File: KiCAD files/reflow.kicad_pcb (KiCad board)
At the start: 2 copper layers, 58.4 x 101.6 mm, 53 parts, among them J1 Screw_Terminal_01x02, J2 Screw_Terminal_01x02, J3 Conn_01x06_Female, J4 Conn_01x06_Female, J5 Conn_01x06_Female, J6 Screw_Terminal_01x02, J7 Screw_Terminal_01x02, U1 MOC3063M, U2 HLK-PM03, U3 ESP-12E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

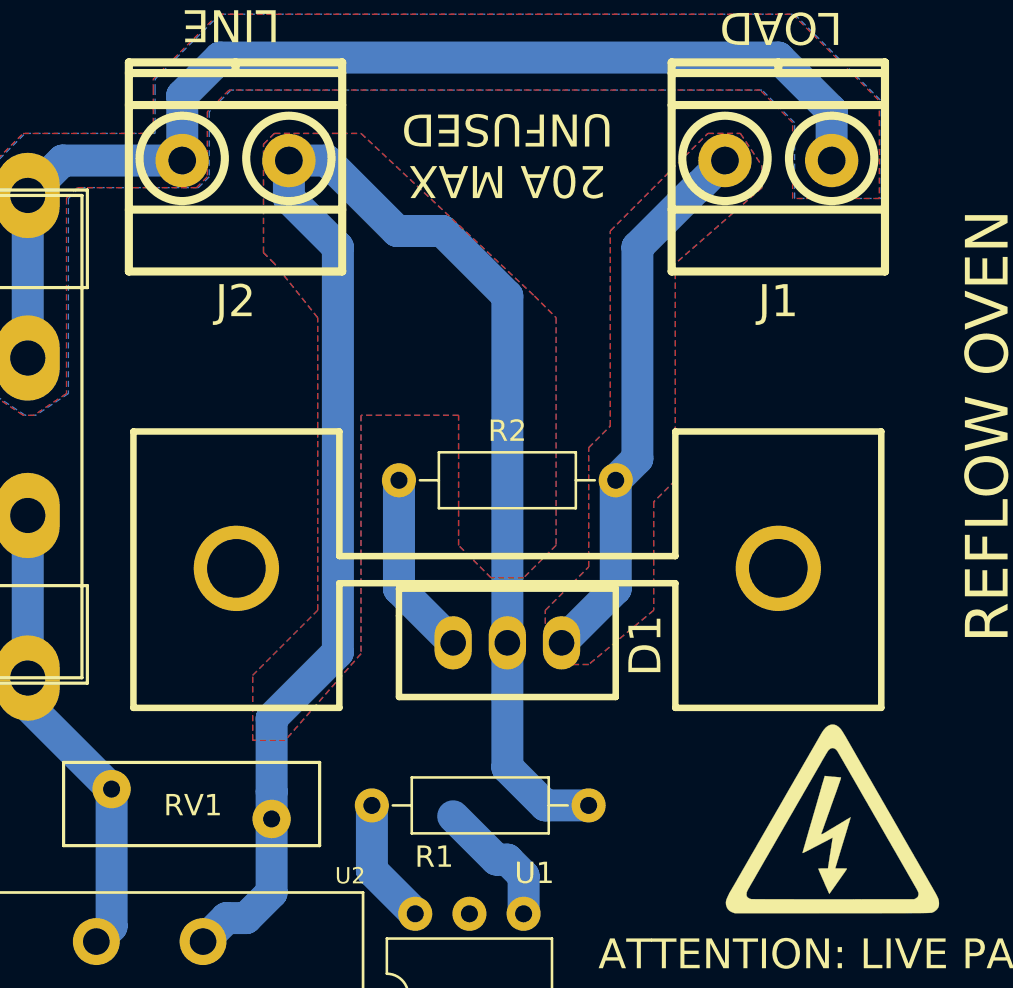
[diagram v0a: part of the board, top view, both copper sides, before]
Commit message: fix triac direction
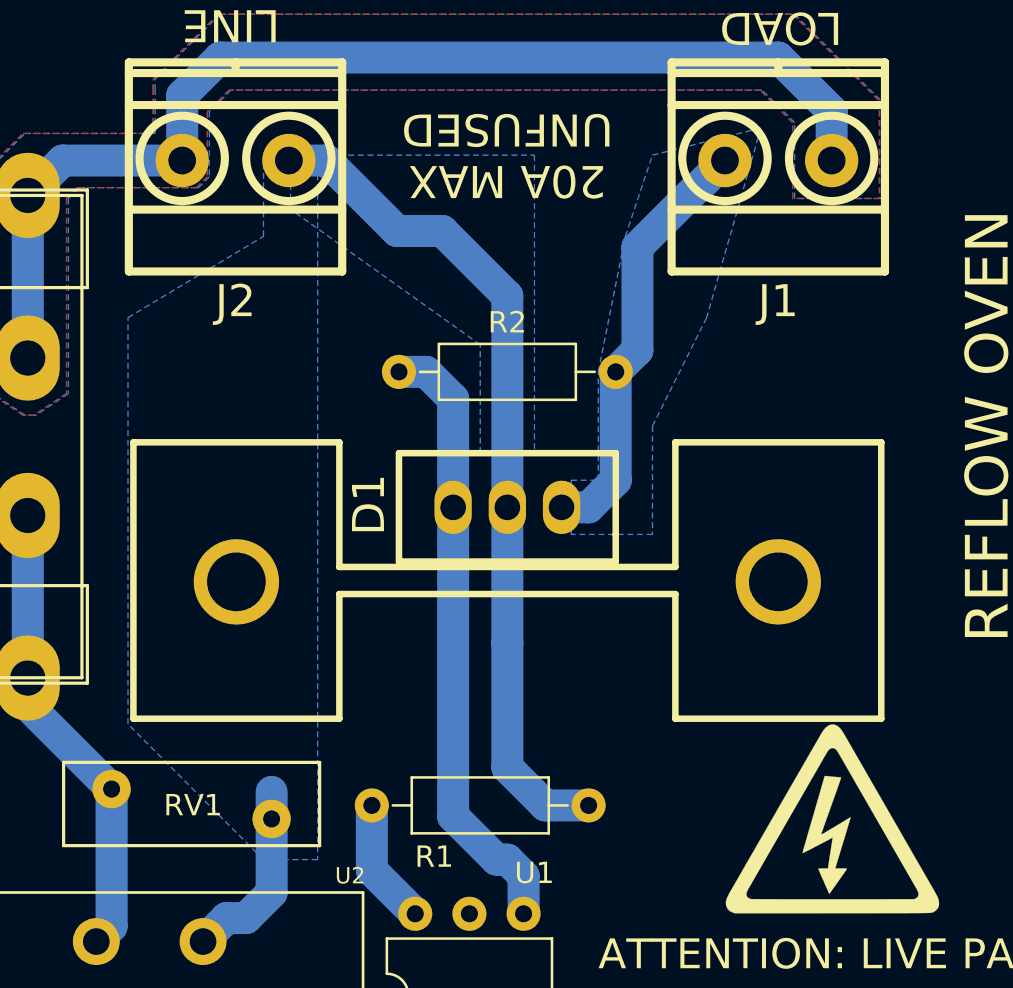
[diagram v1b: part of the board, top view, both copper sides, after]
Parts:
- moved D1 6.35 mm to (151.1, 44.5), turned to 180 degrees
- moved R2 5.08 mm to (146.1, 38.1)
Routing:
- net LIVE: track 80.2 -> 48.4 mm
- net Net-(D1-Pad3): track 14.9 -> 28.9 mm
- net /LOAD: track 25.8 -> 20.2 mm
- removed copper zone on F.Cu, net /LOAD
- removed copper zone on F.Cu, net LIVE
